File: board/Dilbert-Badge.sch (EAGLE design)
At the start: 39 parts, among them IC1 MCP23017SO, J1 IO EXP., J2 FTDI_DEVICE, J3 NEOPIXEL, J5 I2C, SW1 UP, SW2 DOWN, SW3 LEFT, SW4 RIGHT, SW5 A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

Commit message: more layout
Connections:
- net 3V3: now also LED2.VDD, LED3.VDD, LED4.VDD, LED5.VDD, LED6.VDD, LED7.VDD
- net GND: now also LED2.GND, LED3.GND, LED4.GND, LED5.GND, LED6.GND, LED7.GND
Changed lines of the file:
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@@
 <setting verticaltext="up"/>
 </settings>
-<grid distance="0.1" unitdist="inch" unit="inch" style="lines" multiple="1" display="yes" altdistance="0.01" altunitdist="inch" altunit="inch"/>
+<grid distance="0.1" unitdist="inch" unit="inch" style="lines" multiple="1" display="no" altdistance="0.01" altunitdist="inch" altunit="inch"/>
 <layers>
 <layer number="1" name="Top" color="4" fill="1" visible="no" active="no"/>
@@
 <class number="0" name="default" width="0" drill="0">
 </class>
+<class number="1" name="power" width="0.508" drill="0">
+</class>
 </classes>
 <parts>
@@
 </busses>
 <nets>
-<net name="GND" class="0">
+<net name="GND" class="1">
 <segment>
 <pinref part="SW1" gate="G$1" pin="P$1"/>
@@
 <pinref part="LED8" gate="G$1" pin="GND"/>
 <pinref part="LED1" gate="G$1" pin="GND"/>
-<wire x1="248.92" y1="27.94" x2="53.34" y2="27.94" width="0.1524" layer="91"/>
+<wire x1="248.92" y1="27.94" x2="220.98" y2="27.94" width="0.1524" layer="91"/>
+<wire x1="220.98" y1="27.94" x2="193.04" y2="27.94" width="0.1524" layer="91"/>
+<wire x1="193.04" y1="27.94" x2="165.1" y2="27.94" width="0.1524" layer="91"/>
+<wire x1="165.1" y1="27.94" x2="137.16" y2="27.94" width="0.1524" layer="91"/>
+<wire x1="137.16" y1="27.94" x2="109.22" y2="27.94" width="0.1524" layer="91"/>
+<wire x1="109.22" y1="27.94" x2="81.28" y2="27.94" width="0.1524" layer="91"/>
+<wire x1="81.28" y1="27.94" x2="53.34" y2="27.94" width="0.1524" layer="91"/>
 <wire x1="251.46" y1="27.94" x2="248.92" y2="27.94" width="0.1524" layer="91"/>
 <label x="251.46" y="27.94" size="1.778" layer="95"/>
+<pinref part="LED2" gate="G$1" pin="GND"/>
+<junction x="81.28" y="27.94"/>
+<pinref part="LED3" gate="G$1" pin="GND"/>
+<junction x="109.22" y="27.94"/>
+<pinref part="LED5" gate="G$1" pin="GND"/>
+<junction x="165.1" y="27.94"/>
+<pinref part="LED4" gate="G$1" pin="GND"/>
+<junction x="137.16" y="27.94"/>
+<junction x="248.92" y="27.94"/>
+<pinref part="LED7" gate="G$1" pin="GND"/>
+<junction x="220.98" y="27.94"/>
+<pinref part="LED6" gate="G$1" pin="GND"/>
+<junction x="193.04" y="27.94"/>
 </segment>
 <segment>
@@
 </segment>
 </net>
-<net name="3V3" class="0">
+<net name="3V3" class="1">
 <segment>
 <pinref part="R1" gate="G$1" pin="2"/>
@@
 <pinref part="LED1" gate="G$1" pin="VDD"/>
 <pinref part="LED8" gate="G$1" pin="VDD"/>
-<wire x1="58.42" y1="53.34" x2="254" y2="53.34" width="0.1524" layer="91"/>
+<wire x1="58.42" y1="53.34" x2="86.36" y2="53.34" width="0.1524" layer="91"/>
+<wire x1="86.36" y1="53.34" x2="114.3" y2="53.34" width="0.1524" layer="91"/>
+<wire x1="114.3" y1="53.34" x2="142.24" y2="53.34" width="0.1524" layer="91"/>
+<wire x1="142.24" y1="53.34" x2="170.18" y2="53.34" width="0.1524" layer="91"/>
+<wire x1="170.18" y1="53.34" x2="198.12" y2="53.34" width="0.1524" layer="91"/>
+<wire x1="198.12" y1="53.34" x2="226.06" y2="53.34" width="0.1524" layer="91"/>
+<wire x1="226.06" y1="53.34" x2="254" y2="53.34" width="0.1524" layer="91"/>
 <wire x1="256.54" y1="53.34" x2="254" y2="53.34" width="0.1524" layer="91"/>
 <label x="256.54" y="53.34" size="1.778" layer="95"/>
-</segment>
-<segment>
+<pinref part="LED3" gate="G$1" pin="VDD"/>
+<junction x="114.3" y="53.34"/>
+<pinref part="LED2" gate="G$1" pin="VDD"/>
+<junction x="86.36" y="53.34"/>
+<pinref part="LED4" gate="G$1" pin="VDD"/>
+<junction x="142.24" y="53.34"/>
+<pinref part="LED5" gate="G$1" pin="VDD"/>
+<junction x="170.18" y="53.34"/>
+<junction x="254" y="53.34"/>
+<pinref part="LED7" gate="G$1" pin="VDD"/>
+<junction x="226.06" y="53.34"/>
+<pinref part="LED6" gate="G$1" pin="VDD"/>
+<junction x="198.12" y="53.34"/>
+</segment>
+<segment>

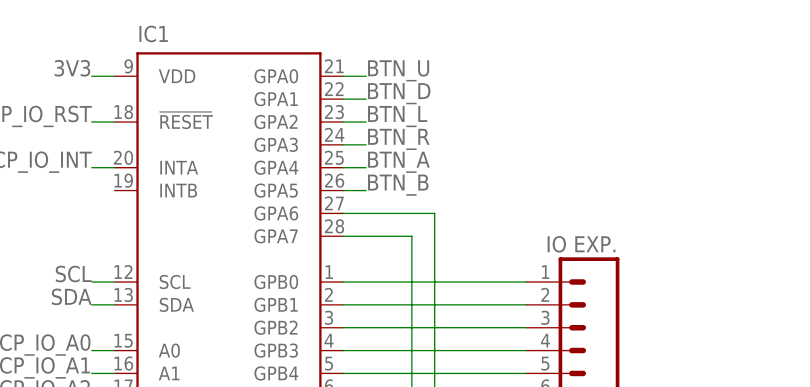
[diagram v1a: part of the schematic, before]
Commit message: correct switches, more layout
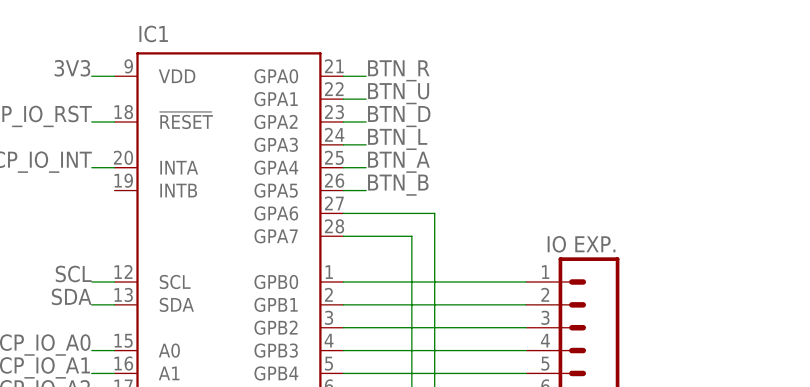
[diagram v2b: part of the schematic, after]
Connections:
- net BTN_D: now also IC1.GPA2; no longer IC1.GPA1
- net BTN_L: now also IC1.GPA3; no longer IC1.GPA2
- net BTN_R: now also IC1.GPA0; no longer IC1.GPA3
- net BTN_U: now also IC1.GPA1; no longer IC1.GPA0
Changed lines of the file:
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@@
 </segment>
 <segment>
-<pinref part="IC1" gate="G$1" pin="GPA0"/>
-<label x="76.2" y="233.68" size="1.778" layer="95"/>
-<wire x1="73.66" y1="233.68" x2="76.2" y2="233.68" width="0.1524" layer="91"/>
+<pinref part="IC1" gate="G$1" pin="GPA1"/>
+<label x="76.2" y="231.14" size="1.778" layer="95"/>
+<wire x1="76.2" y1="231.14" x2="73.66" y2="231.14" width="0.1524" layer="91"/>
 </segment>
 </net>
@@
 </segment>
 <segment>
-<pinref part="IC1" gate="G$1" pin="GPA1"/>
-<label x="76.2" y="231.14" size="1.778" layer="95"/>
-<wire x1="76.2" y1="231.14" x2="73.66" y2="231.14" width="0.1524" layer="91"/>
+<pinref part="IC1" gate="G$1" pin="GPA2"/>
+<label x="76.2" y="228.6" size="1.778" layer="95"/>
+<wire x1="73.66" y1="228.6" x2="76.2" y2="228.6" width="0.1524" layer="91"/>
 </segment>
 </net>
@@
 </segment>
 <segment>
-<pinref part="IC1" gate="G$1" pin="GPA2"/>
-<label x="76.2" y="228.6" size="1.778" layer="95"/>
-<wire x1="73.66" y1="228.6" x2="76.2" y2="228.6" width="0.1524" layer="91"/>
+<pinref part="IC1" gate="G$1" pin="GPA3"/>
+<label x="76.2" y="226.06" size="1.778" layer="95"/>
+<wire x1="76.2" y1="226.06" x2="73.66" y2="226.06" width="0.1524" layer="91"/>
 </segment>
 </net>
@@
 </segment>
 <segment>
-<pinref part="IC1" gate="G$1" pin="GPA3"/>
-<label x="76.2" y="226.06" size="1.778" layer="95"/>
-<wire x1="76.2" y1="226.06" x2="73.66" y2="226.06" width="0.1524" layer="91"/>
+<pinref part="IC1" gate="G$1" pin="GPA0"/>
+<label x="76.2" y="233.68" size="1.778" layer="95"/>
+<wire x1="73.66" y1="233.68" x2="76.2" y2="233.68" width="0.1524" layer="91"/>
 </segment>
 </net>

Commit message: ERC/DRU checks
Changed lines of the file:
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@@
 <pinref part="SW3" gate="G$1" pin="P$1"/>
 <junction x="35.56" y="149.86"/>
+<junction x="35.56" y="139.7"/>
 </segment>
 <segment>
@@
 <label x="68.58" y="134.62" size="1.778" layer="95" rot="MR180"/>
 <wire x1="68.58" y1="139.7" x2="68.58" y2="134.62" width="0.1524" layer="91"/>
+<junction x="68.58" y="139.7"/>
 </segment>
 <segment>
@@
 <label x="114.3" y="152.4" size="1.778" layer="95"/>
 <pinref part="R1" gate="G$1" pin="1"/>
+<junction x="109.22" y="152.4"/>
 </segment>
 </net>
@@
 <wire x1="137.16" y1="152.4" x2="132.08" y2="152.4" width="0.1524" layer="91"/>
 <pinref part="R5" gate="G$1" pin="1"/>
+<junction x="132.08" y="152.4"/>
 </segment>
 </net>
@@
 </sheet>
 </sheets>
+<errors>
+</errors>
 </schematic>
 </drawing>

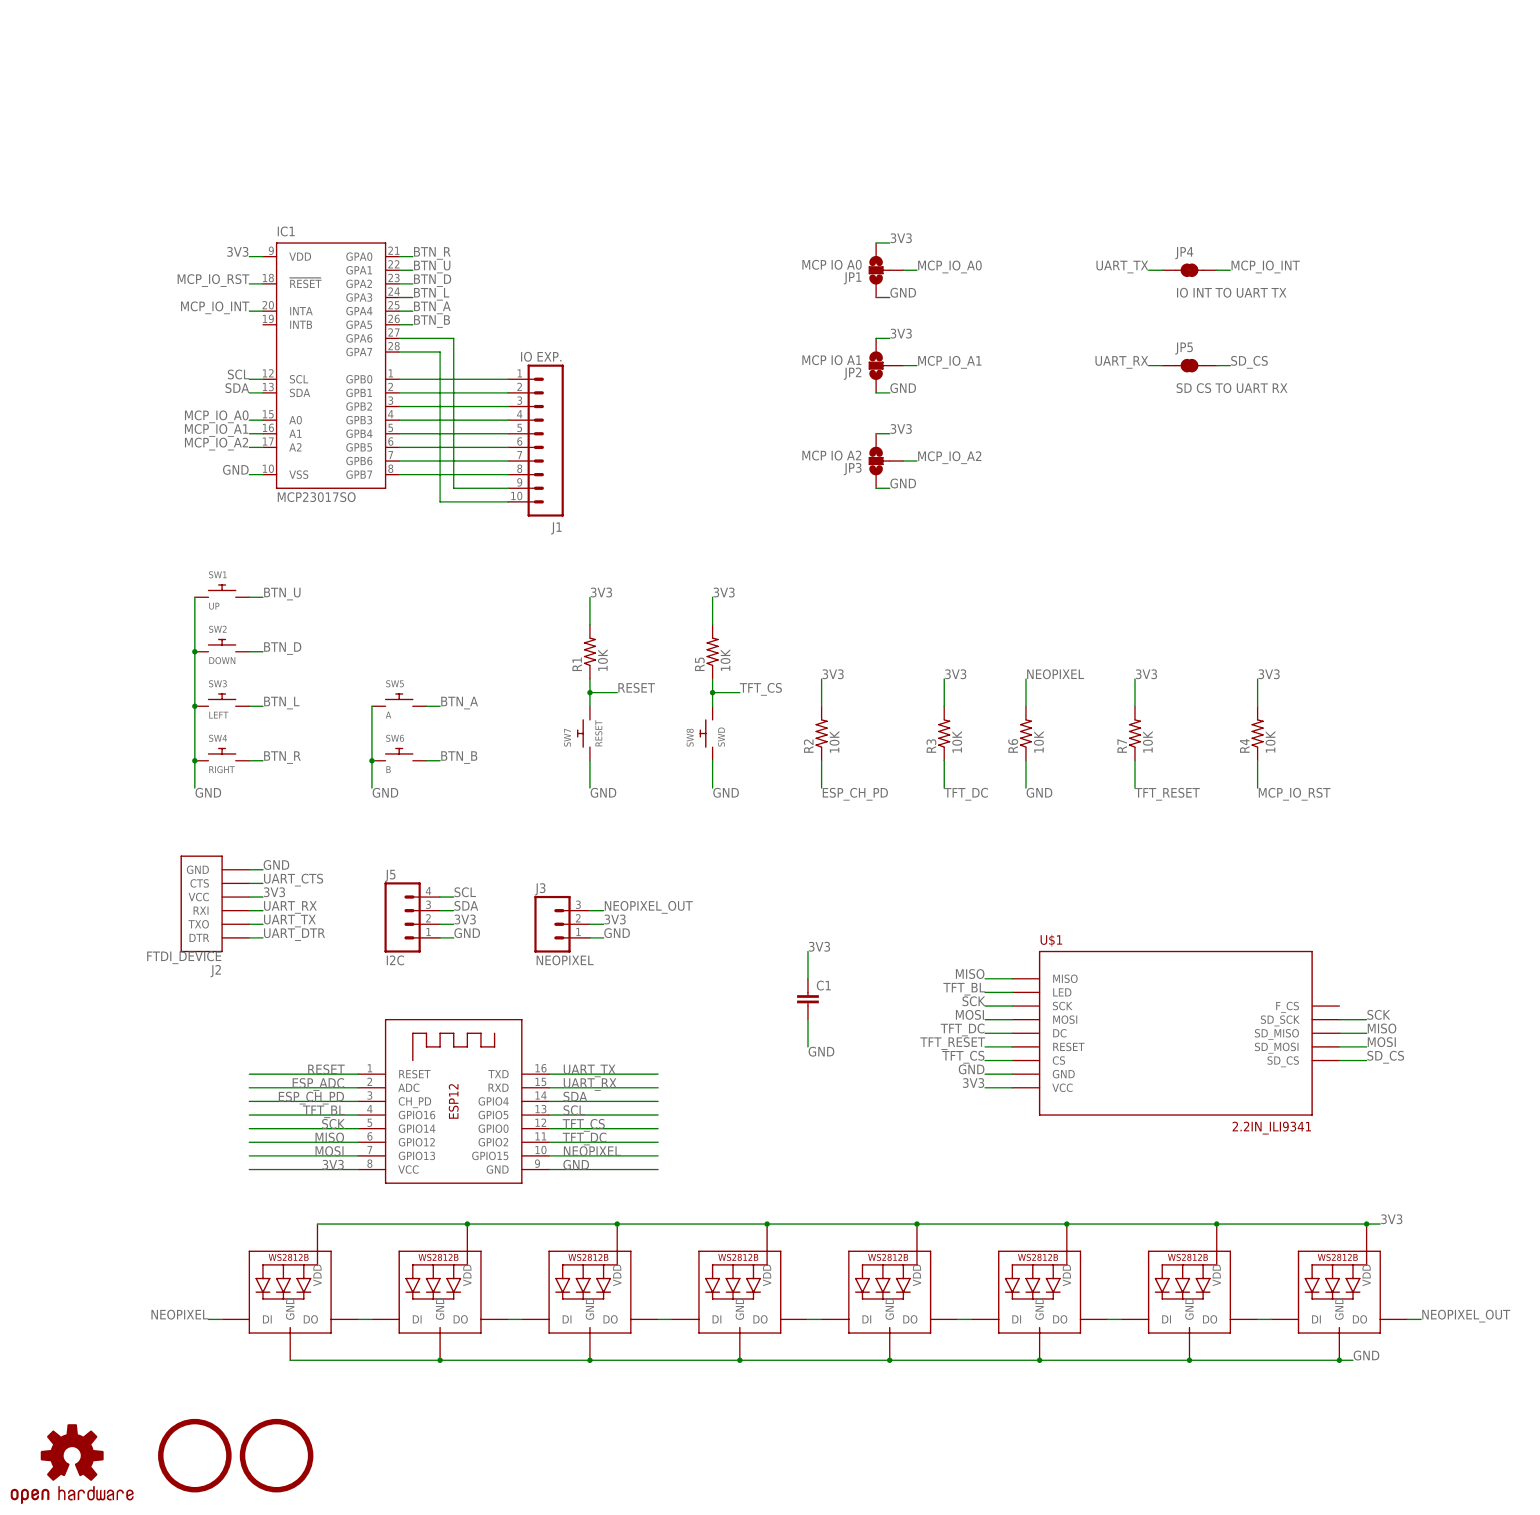
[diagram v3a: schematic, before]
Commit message: add regulator, tidy layout
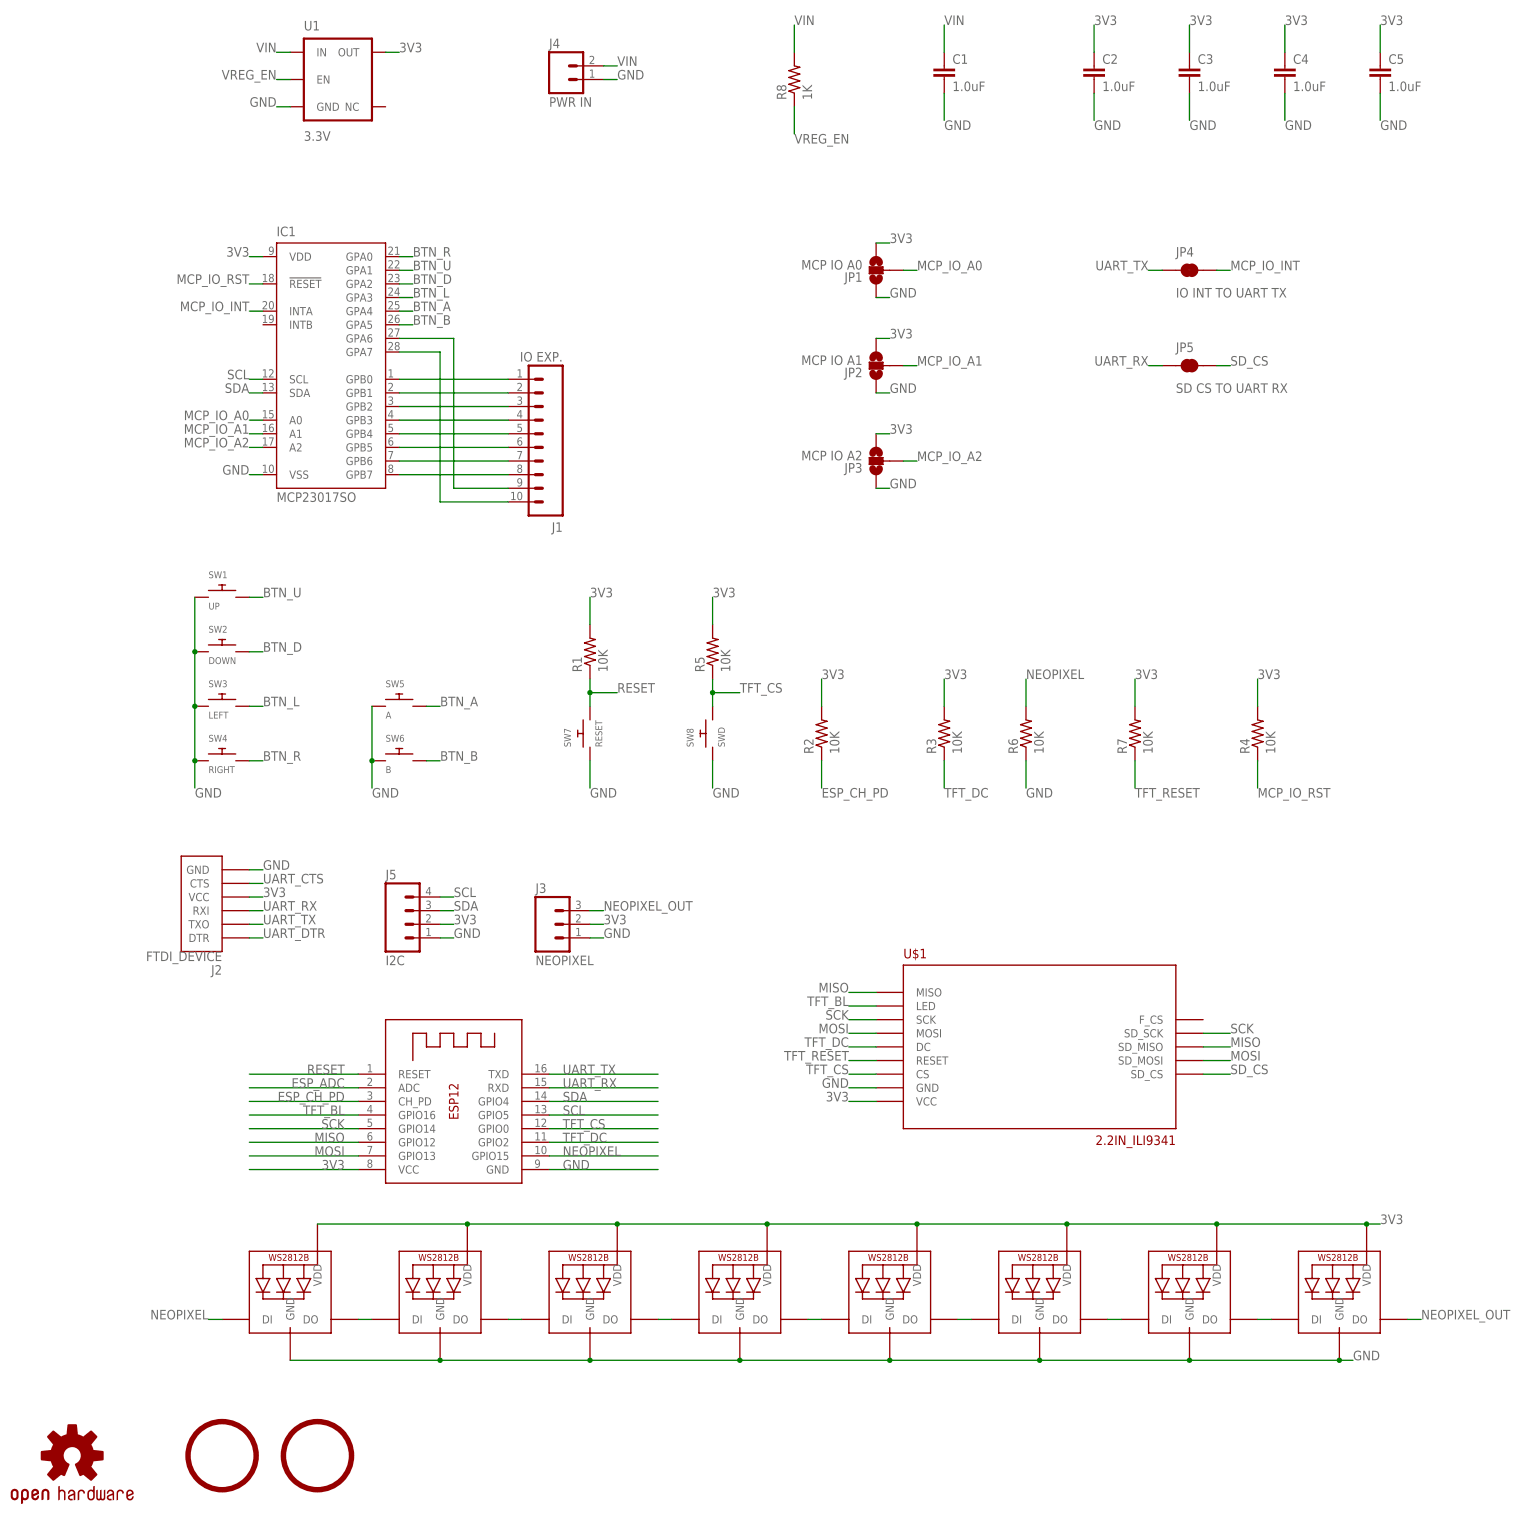
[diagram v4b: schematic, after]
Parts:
- added C2, C3, C4, C5: 1.0uF, SparkFun-Capacitors:1.0UF-25V-+80/-20(0805)"
- added J4: PWR IN, SparkFun-Connectors:M02PTH
- added R8: 1K, adafruit:R-US_R0805
- added U1: 3.3V, SparkFun-PowerIC:V_REG_AP2112K-3.3V
- C1: value (none) -> 1.0uF; device SparkFun-Capacitors:10UF10V10%(0805) -> SparkFun-Capacitors:1.0UF-25V-+80/-20(0805)"
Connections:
- new net VIN: C1.1, J4.2, R8.2, U1.IN
- new net VREG_EN: R8.1, U1.EN
- net 3V3: now also C2.1, C3.1, C4.1, C5.1, U1.OUT; no longer C1.1
- net GND: now also C2.2, C3.2, C4.2, C5.2, J4.1, U1.GND
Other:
- moved on the sheet: C1, U$1

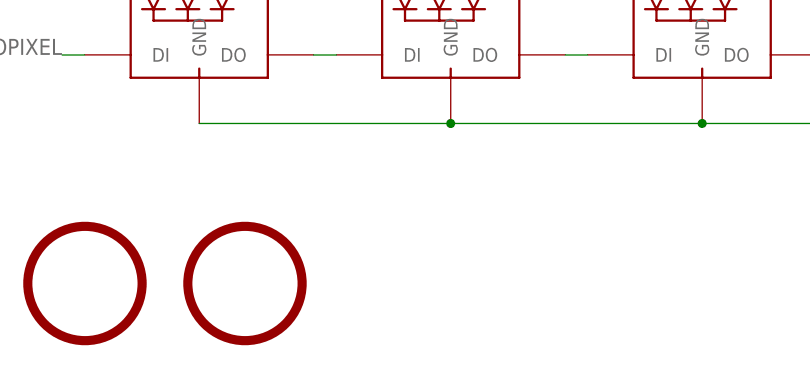
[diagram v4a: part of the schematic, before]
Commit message: add hole for landscape lanyard
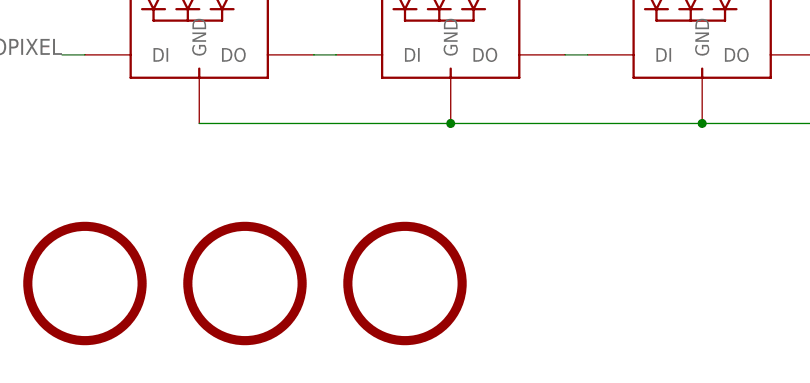
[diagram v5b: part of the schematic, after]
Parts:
- added U$4: 5MM_MOUNTING_HOLE, mechanical:5MM_MOUNTING_HOLE
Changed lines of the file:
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@@
 <setting verticaltext="up"/>
 </settings>
-<grid distance="0.1" unitdist="inch" unit="inch" style="lines" multiple="1" display="yes" altdistance="0.01" altunitdist="inch" altunit="inch"/>
+<grid distance="0.1" unitdist="inch" unit="inch" style="lines" multiple="1" display="no" altdistance="0.01" altunitdist="inch" altunit="inch"/>
 <layers>
 <layer number="1" name="Top" color="4" fill="1" visible="no" active="no"/>
@@
 <part name="C4" library="SparkFun-Capacitors" deviceset="1.0UF-25V-+80/-20(0805)" device="&quot;" value="1.0uF"/>
 <part name="C5" library="SparkFun-Capacitors" deviceset="1.0UF-25V-+80/-20(0805)" device="&quot;" value="1.0uF"/>
+<part name="U$4" library="mechanical" deviceset="5MM_MOUNTING_HOLE" device=""/>
 </parts>
 <sheets>
@@
 <instance part="C4" gate="G$1" x="238.76" y="266.7"/>
 <instance part="C5" gate="G$1" x="256.54" y="266.7"/>
+<instance part="U$4" gate="G$1" x="76.2" y="10.16"/>
 </instances>
 <busses>
